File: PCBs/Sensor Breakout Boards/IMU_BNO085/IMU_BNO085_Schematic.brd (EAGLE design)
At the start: 26.7 x 35.6 mm, 8 parts, among them J1 2X6 FEMALE

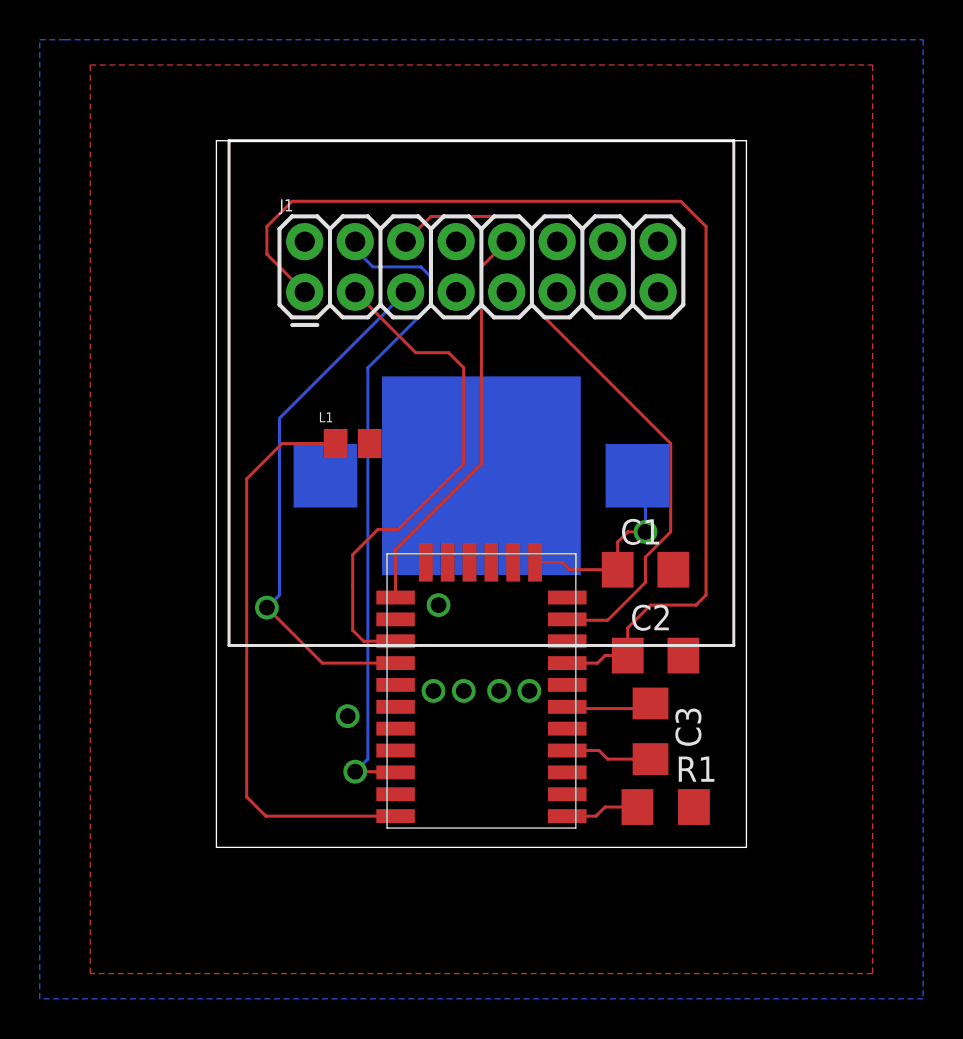
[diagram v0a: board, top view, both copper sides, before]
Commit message: fix standby and gnd gps
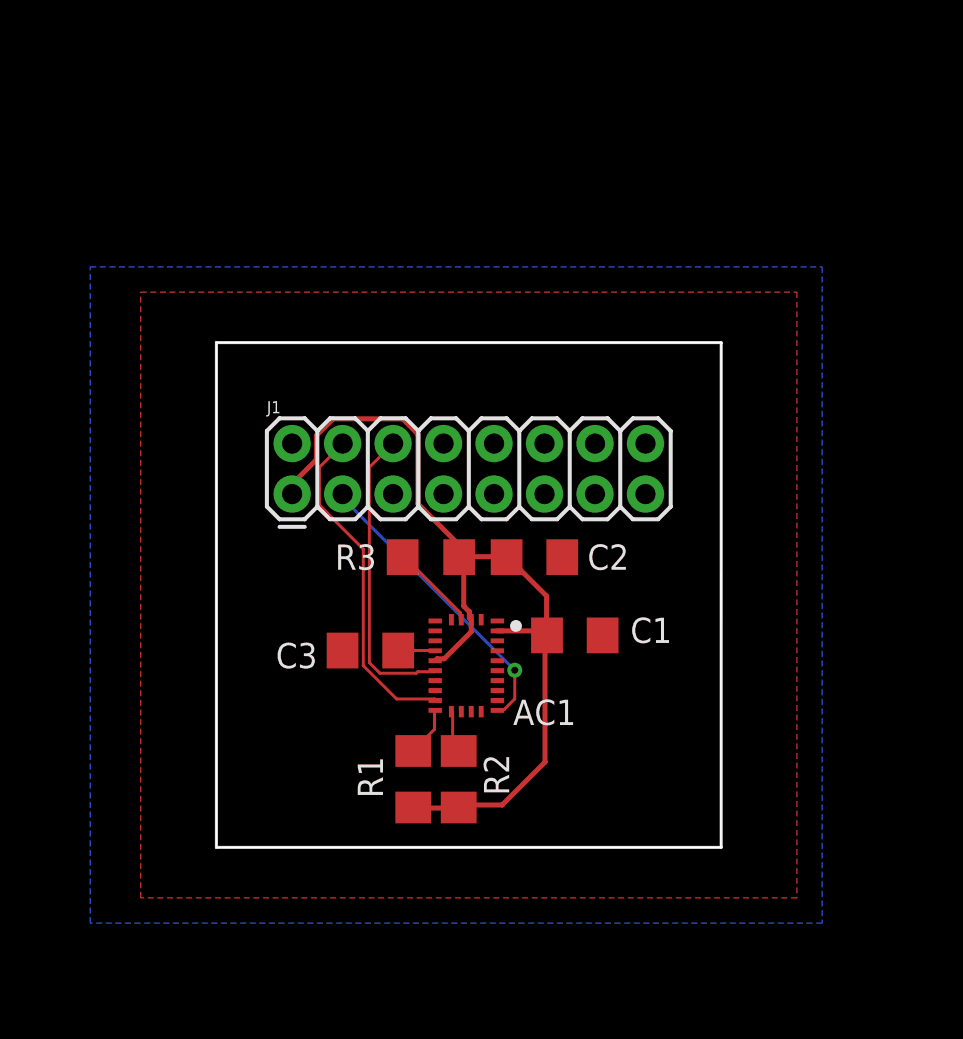
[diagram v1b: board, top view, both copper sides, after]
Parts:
- removed A1: (no value), M20050-1 GPS:M20050-1_GPS
- removed B1: 3000K, b_keystone_3000k_sm_battery:3000K
- removed L1: 1.8n, AIMC-0805-1N8S-T:INDC2012X105N
- added AC1: BNO085, BNO085:BNO085
- added R2: 2.2k, RTR Main Library:R1206
- added R3: 10k, RTR Main Library:R1206
- C1, C3: value 22p -> 0.1u
- C2: value 2.2u -> 0.1u
- R1: value 0R -> 2.2k
- moved C3 14.7 mm to (7.75, 9.91), turned to 180 degrees
- moved R1 12.8 mm to (9.91, 3.43), turned to 270 degrees
- moved J1 10.2 mm to (12.7, 12.7)
- moved C2 7.85 mm to (16.0, 14.6)
- moved C1 4.85 mm to (18.0, 10.7)
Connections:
- removed net BV: A1.P12, B1.+, C1.1
- removed net FIX: A1.P18, J1.10
- removed net N$4: A1.P28, L1.1
- removed net RX: A1.P21, J1.5
- removed net STB: A1.P26, J1.4
- removed net TX: A1.P20, J1.3
- new net 5V: J1.2
- new net INT: AC1.14, J1.4
- new net N$8: AC1.4, R3.1
- new net SCL: AC1.19, J1.5
- new net SDA: AC1.20, J1.3
- net GND: now also AC1.17, AC1.2, AC1.25, AC1.26, AC1.5, AC1.6, C3.2; no longer A1.P15, A1.P16, A1.P17, A1.P19, A1.P2, A1.P22, A1.P23, A1.P24, A1.P25, A1.P27, A1.P3, A1.P5, A1.P7, A1.P9, B1.-, L1.2, R1.2
- net N$1: now also AC1.16, R2.1; no longer A1.P6, C3.1
- net N$2: now also AC1.15, R1.1; no longer A1.P4, C3.2
- net N$3: now also AC1.9, C3.1; no longer A1.P1, R1.1
- net RST: now also AC1.11; no longer A1.P10
- net VCC: now also AC1.10, AC1.28, AC1.3, C1.1, R1.2, R2.2, R3.2; no longer A1.P8
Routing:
- net STB: track 33.3 -> 0.00 mm, vias 1 -> 0
- net N$4: track 29.1 -> 0.00 mm
- net RX: track 26.4 -> 0.00 mm, vias 1 -> 0
- net TX: track 25.5 -> 0.00 mm
- net FIX: track 20.2 -> 0.00 mm
- net RST: track 33.1 -> 15.1 mm
- net INT: track 0.00 -> 16.9 mm
- net SDA: track 0.00 -> 15.0 mm, vias 0 -> 1
- net BV: track 10.4 -> 0.00 mm, vias 1 -> 0
- net VCC: track 55.0 -> 46.5 mm
- net N$8: track 0.00 -> 4.45 mm
- net N$1: track 4.32 -> 2.14 mm
- net N$2: track 4.37 -> 2.50 mm
- net N$3: track 3.72 -> 1.86 mm
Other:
- board size 26.7 x 35.6 mm -> 25.4 x 25.4 mm
